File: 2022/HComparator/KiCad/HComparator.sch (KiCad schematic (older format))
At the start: 22 parts, among them M1 PMOS_OR1, M10 NMOS_OR1, M11 NMOS_OR1, M12 PMOS_OR1, M13 NMOS_OR1, M14 NMOS_OR1, M15 PMOS_OR1, M16 NMOS_OR1, M17 PMOS_OR1, M18 NMOS_OR1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

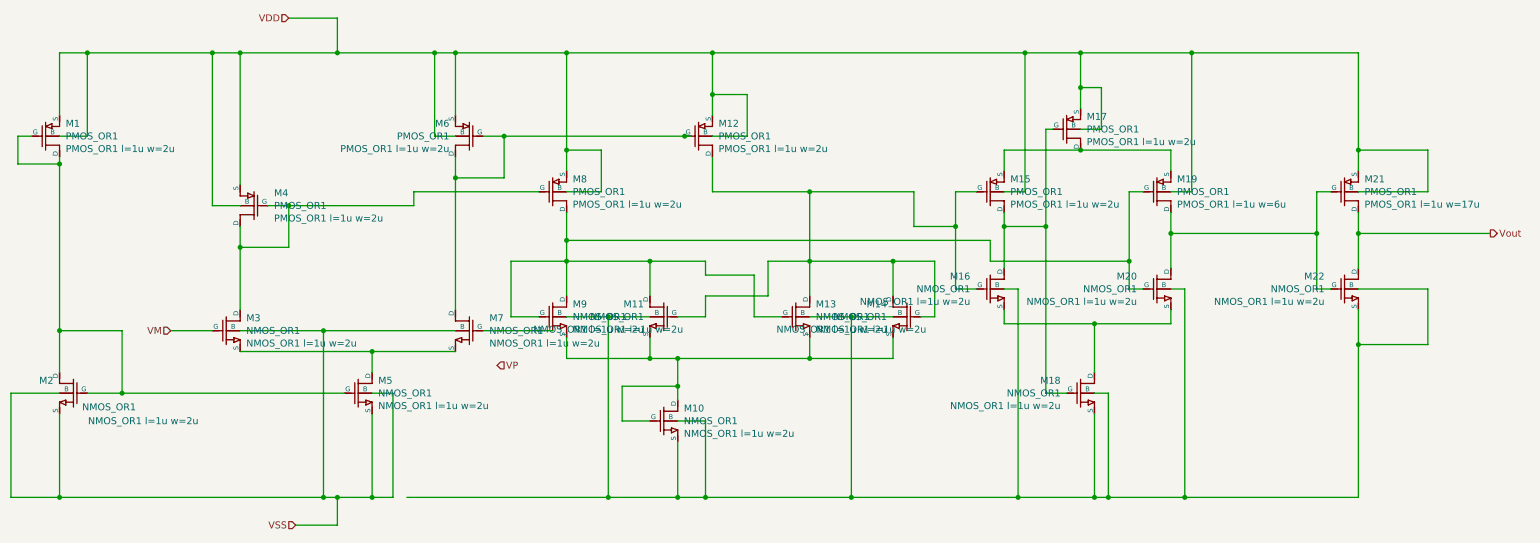
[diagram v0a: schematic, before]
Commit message: cross はテストのために仮に作ったものでいらなかった。
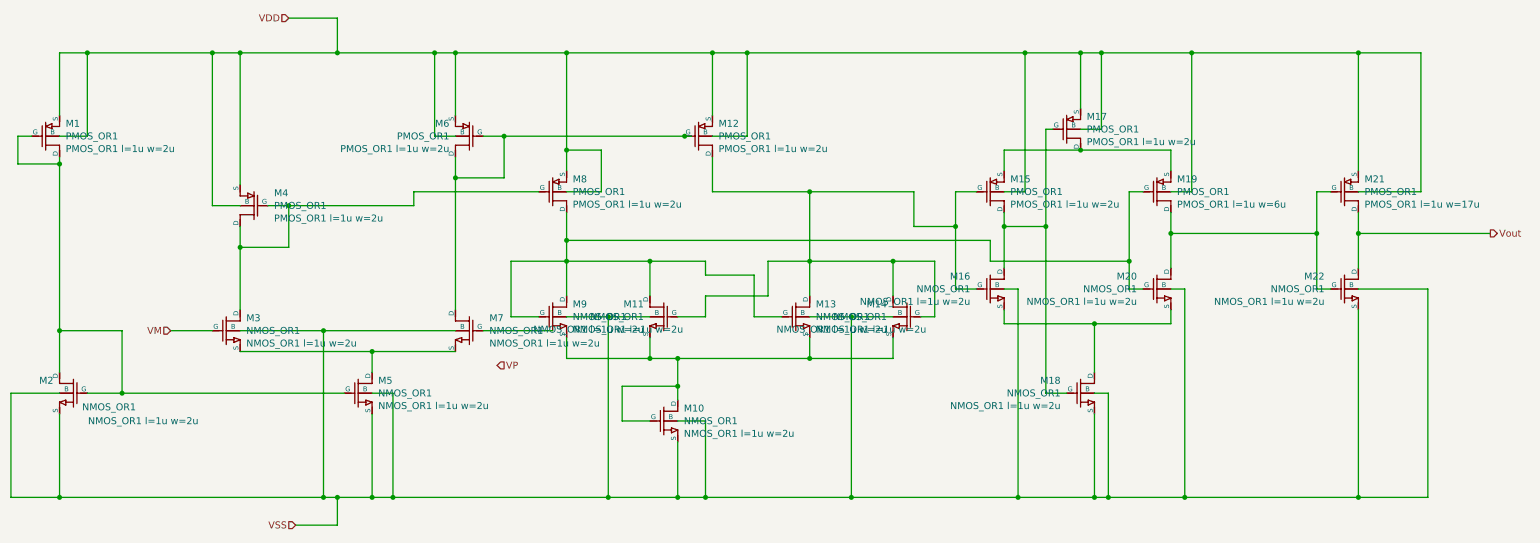
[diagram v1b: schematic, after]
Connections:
- net VSS: now also M10.3 (S), M10.4 (B), M11.4 (B), M13.4 (B), M14.4 (B), M16.4 (B), M18.3 (S), M18.4 (B), M20.4 (B), M22.3 (S), M22.4 (B), M9.4 (B)
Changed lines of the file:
@@
 Connection ~ 8850 4450
 Wire Wire Line
-	10100 3100 10100 3350
-Wire Wire Line
 	10100 2950 10600 2950
-Wire Wire Line
-	10600 2950 10600 3350
-Wire Wire Line
-	10600 3350 10100 3350
-Connection ~ 10100 3350
-Wire Wire Line
-	10100 3350 10100 4450
 Wire Wire Line
 	8200 3850 8200 4450
@@
 Wire Wire Line
 	6750 2750 6750 3000
-Wire Wire Line
-	3250 4450 4700 4450
 Connection ~ 4700 4450
 Wire Wire Line
@@
 Connection ~ 5450 1250
 Wire Wire Line
-	5450 1250 7700 1250
+	5450 1250 5700 1250
 Wire Wire Line
 	8900 2250 8750 2250
@@
 	7550 2500 7850 2500
 Wire Wire Line
-	8250 1500 8250 1800
-Wire Wire Line
 	8100 1950 8750 1950
 Wire Wire Line
@@
 Wire Wire Line
 	8900 1250 10100 1250
-Wire Wire Line
-	10100 1250 10100 1950
-Wire Wire Line
-	10100 1950 10600 1950
-Wire Wire Line
-	10600 1950 10600 2250
-Wire Wire Line
-	10100 2250 10600 2250
-Connection ~ 10100 1950
-Wire Wire Line
-	10100 1950 10100 2100
 Text HLabel 11050 2550 2    50   Output ~ 0
 Vout
@@
 	7200 2250 7200 2500
 Wire Wire Line
-	8100 1500 8100 1650
-Wire Wire Line
-	8100 1500 8250 1500
-Wire Wire Line
 	7700 1250 7700 2250
 Connection ~ 7700 1250
 Wire Wire Line
 	7700 1250 8100 1250
-Connection ~ 8100 1500
-Wire Wire Line
-	8100 1250 8100 1500
 Connection ~ 8100 1250
 Connection ~ 8900 1250
-Wire Wire Line
-	8900 1250 8100 1250
 Connection ~ 4400 2600
 Wire Wire Line
@@
 Wire Wire Line
 	5700 1850 5450 1850
-Wire Wire Line
-	5700 1550 5700 1850
-Wire Wire Line
-	5450 1250 5450 1550
-Wire Wire Line
-	5450 1550 5450 1700
-Connection ~ 5450 1550
-Wire Wire Line
-	5450 1550 5700 1550
 Wire Wire Line
 	5450 2000 5450 2250
@@
 Wire Wire Line
 	5200 4050 5200 4450
+Wire Wire Line
+	3150 4450 4700 4450
+Connection ~ 3150 4450
+Wire Wire Line
+	5450 1250 5450 1700
+Wire Wire Line
+	5700 1850 5700 1250
+Connection ~ 5700 1250
+Wire Wire Line
+	5700 1250 7700 1250
+Wire Wire Line
+	8100 1250 8100 1650
+Wire Wire Line
+	8250 1800 8250 1250
+Wire Wire Line
+	8100 1250 8250 1250
+Connection ~ 8250 1250
+Wire Wire Line
+	8250 1250 8900 1250
+Wire Wire Line
+	10100 1250 10100 2100
+Wire Wire Line
+	10100 1250 10550 1250
+Wire Wire Line
+	10550 1250 10550 2250
+Wire Wire Line
+	10100 2250 10550 2250
+Connection ~ 10100 1250
+Wire Wire Line
+	10100 3100 10100 4450
+Wire Wire Line
+	10600 2950 10600 4450
+Wire Wire Line
+	10600 4450 10100 4450
+Connection ~ 10100 4450
 $EndSCHEMATC

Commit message: ディレクトリ名の変更
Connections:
- net VSS: no longer M10.3 (S), M10.4 (B), M11.4 (B), M13.4 (B), M14.4 (B), M16.4 (B), M18.3 (S), M18.4 (B), M20.4 (B), M22.3 (S), M22.4 (B), M9.4 (B)
- new net: M10.3 (S), M10.4 (B), M11.4 (B), M13.4 (B), M14.4 (B), M16.4 (B), M18.3 (S), M18.4 (B), M20.4 (B), M22.3 (S), M22.4 (B), M9.4 (B)

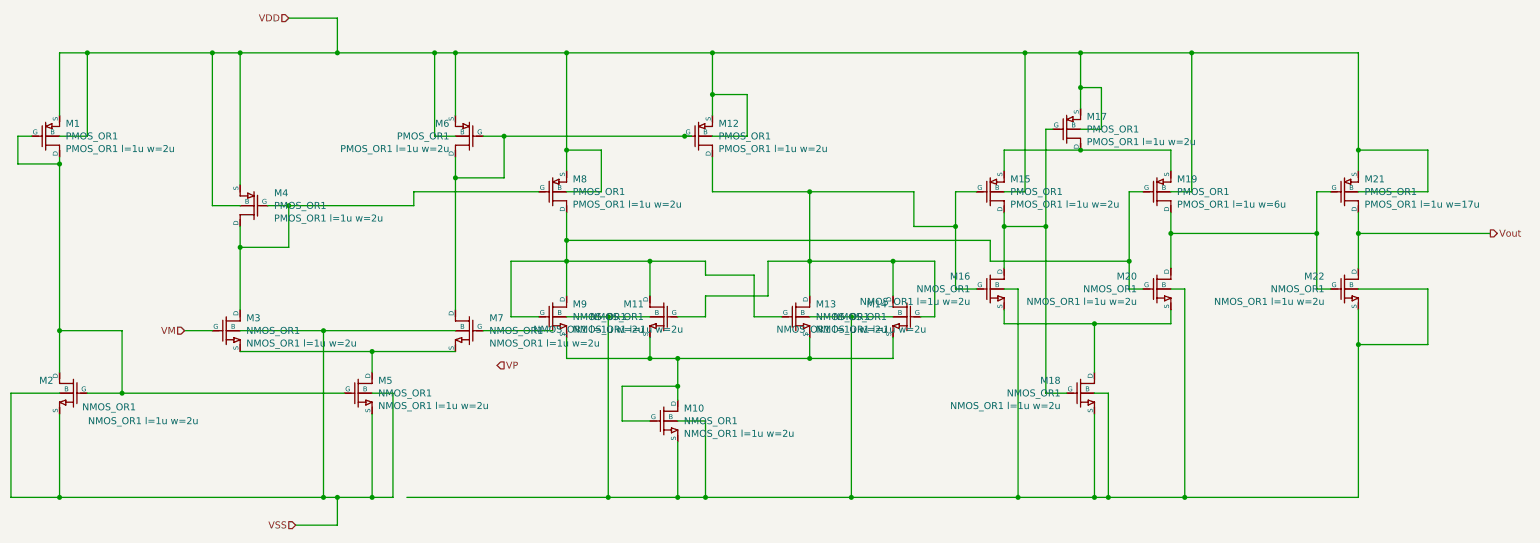
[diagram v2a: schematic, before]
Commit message: KiCad の分割した回路図でも LVS が通るようになった。 シート名称にブランクを入れてはいけない。
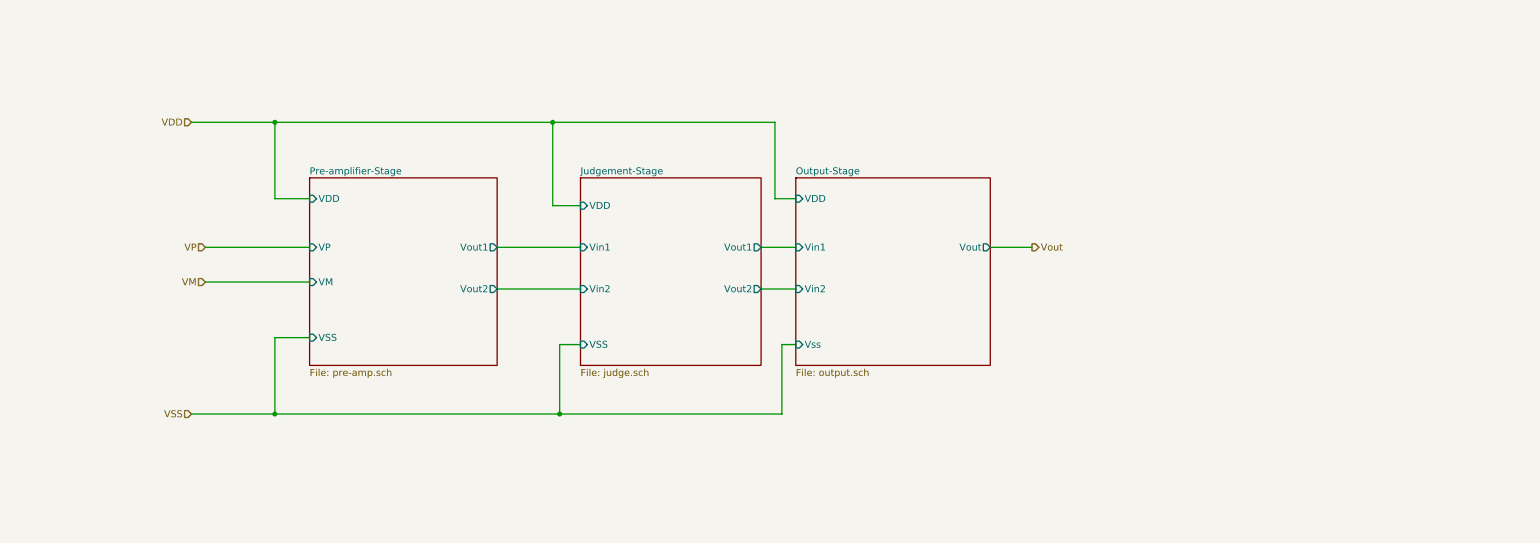
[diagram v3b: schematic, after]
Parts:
- removed M1, M12, M15, M17, M19, M21, M4, M6, M8: PMOS_OR1, symbol 0_OR1Symbols:PMOS_OR1
- removed M10, M11, M13, M14, M16, M18, M2, M20, M22, M3, M5, M7, M9: NMOS_OR1, symbol 0_OR1Symbols:NMOS_OR1
